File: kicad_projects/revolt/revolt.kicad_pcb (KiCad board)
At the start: 2 copper layers, 144.9 x 111.9 mm, 69 parts, among them J1 IDC-Header_2x07_P2.54mm_Verti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

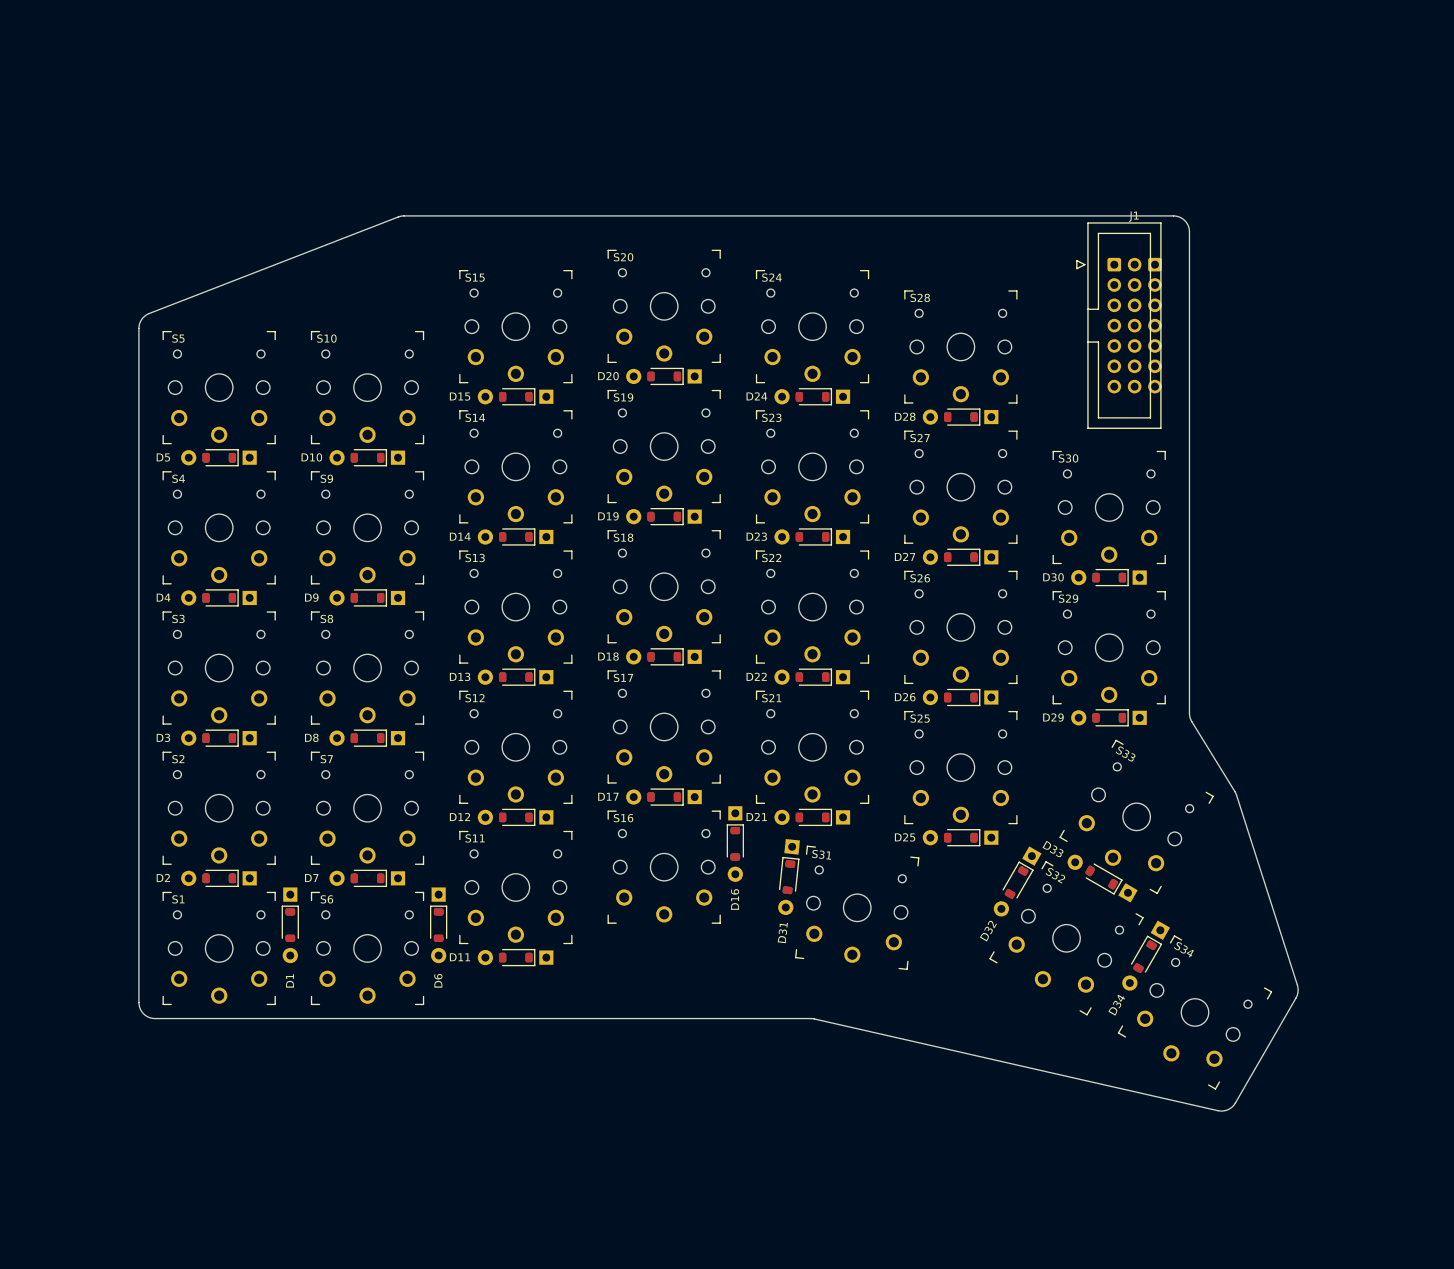
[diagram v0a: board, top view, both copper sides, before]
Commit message: Improved diodes, LED schematic
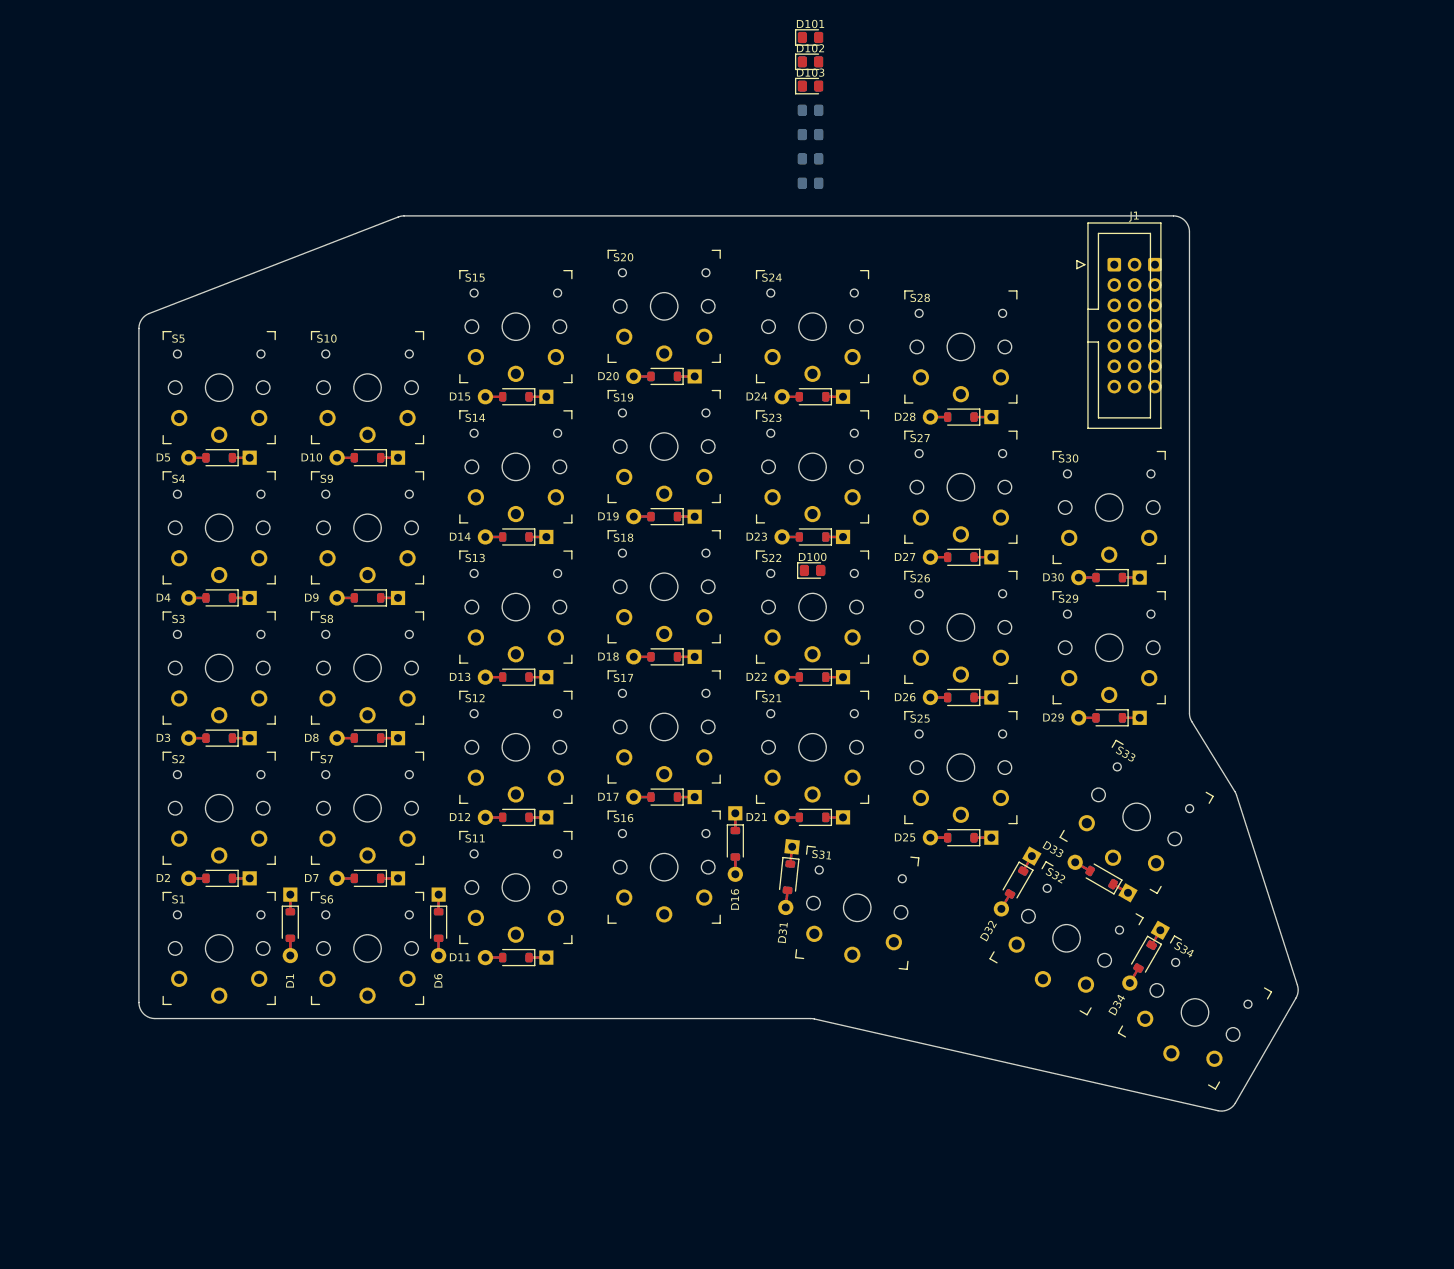
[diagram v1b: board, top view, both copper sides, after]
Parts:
- added D100: LED, LED_SMD:LED_0805_2012Metric_Pad1.15x1.40mm_HandSolder, F.Cu at (175.8, 105.2)
- added D101: LED, LED_SMD:LED_0805_2012Metric_Pad1.15x1.40mm_HandSolder, F.Cu at (175.5, 38.5)
- added D102: LED, LED_SMD:LED_0805_2012Metric_Pad1.15x1.40mm_HandSolder, F.Cu at (175.5, 41.6)
- added D103: LED, LED_SMD:LED_0805_2012Metric_Pad1.15x1.40mm_HandSolder, F.Cu at (175.5, 44.6)
- added D104: LED, LED_SMD:LED_0805_2012Metric_Pad1.15x1.40mm_HandSolder, B.Cu at (175.5, 56.7)
- added D105: LED, LED_SMD:LED_0805_2012Metric_Pad1.15x1.40mm_HandSolder, B.Cu at (175.5, 53.7)
- added D106: LED, LED_SMD:LED_0805_2012Metric_Pad1.15x1.40mm_HandSolder, B.Cu at (175.5, 50.7)
- added D107: LED, LED_SMD:LED_0805_2012Metric_Pad1.15x1.40mm_HandSolder, B.Cu at (175.5, 47.6)

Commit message: Final footprints, schematic fixes, LEDs positioned
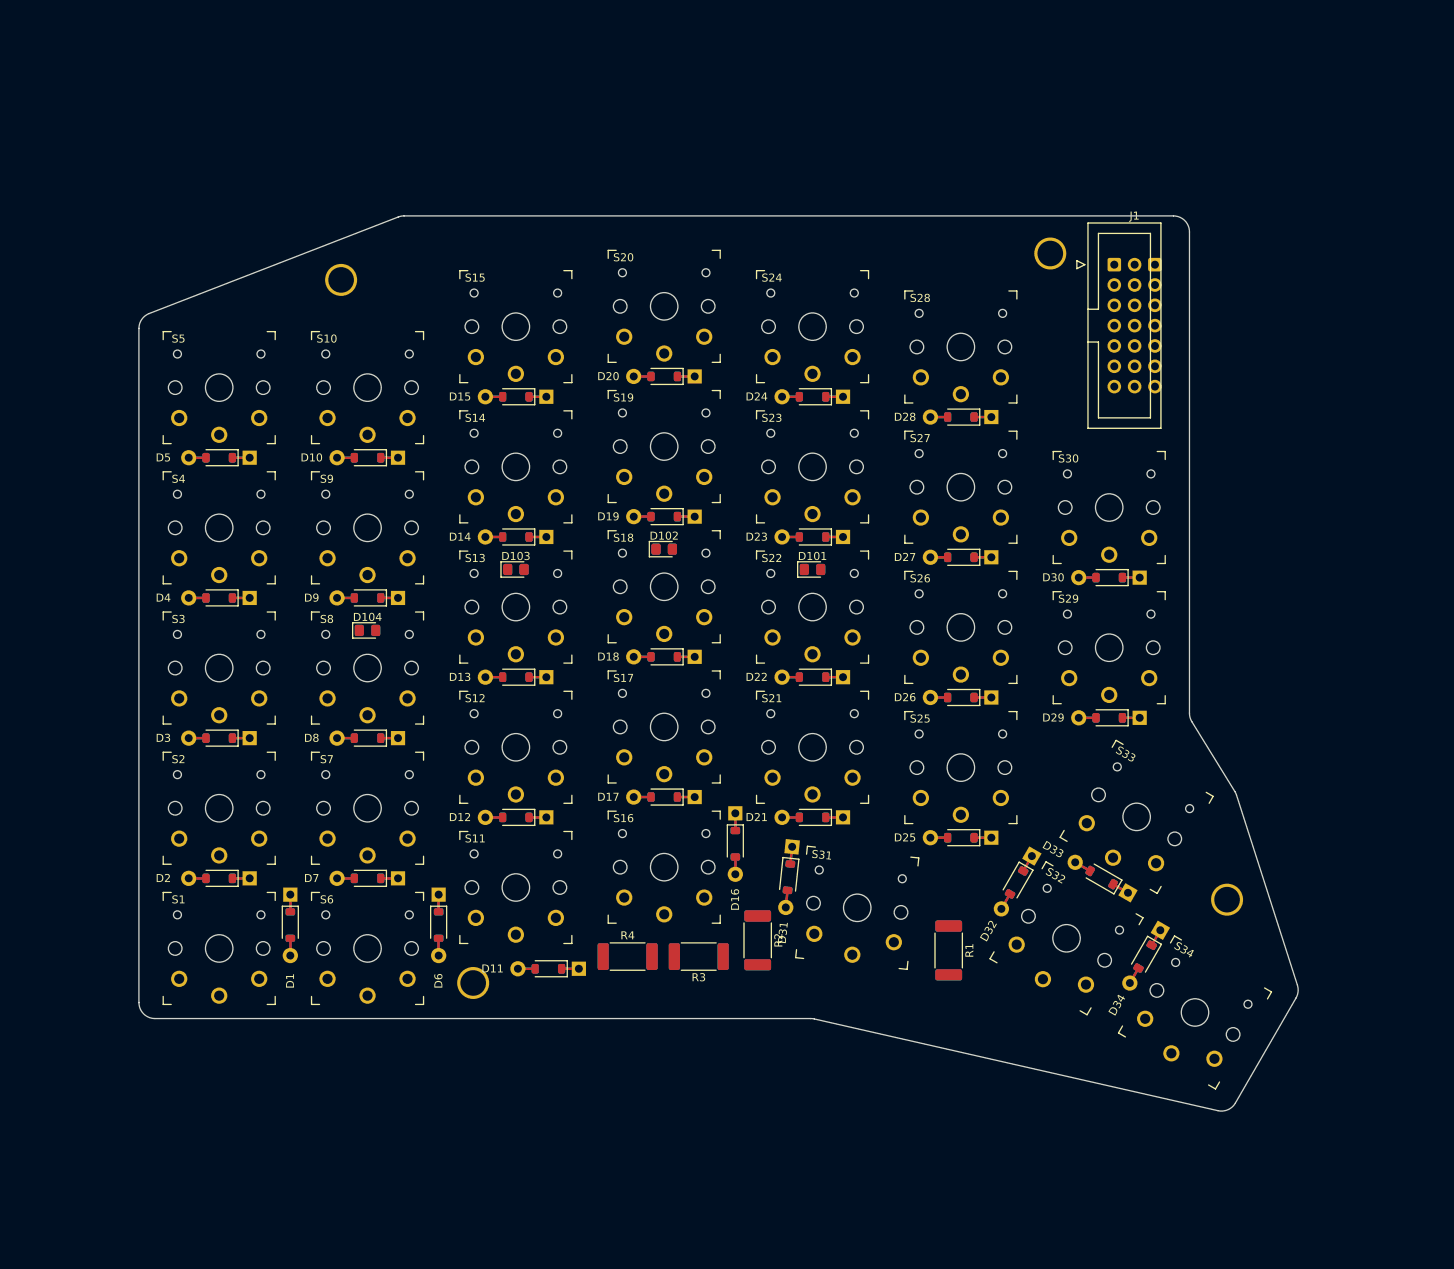
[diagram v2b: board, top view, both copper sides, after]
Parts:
- added H1: MountingHole, revolt_footprints:HOLE_M3, F.Cu at (116.8, 68.8)
- added H2: MountingHole, revolt_footprints:HOLE_M3, F.Cu at (205.5, 65.5)
- added H3: MountingHole, revolt_footprints:HOLE_M3, F.Cu at (227.6, 146.3)
- added H4: MountingHole, revolt_footprints:HOLE_M3, F.Cu at (133.3, 156.7)
- added R1: 150, revolt_footprints:R_2512_6332Metric_Pad1.40x3.35mm_HandSolder_reversible, F.Cu at (192.8, 152.7)
- added R2: 150, revolt_footprints:R_2512_6332Metric_Pad1.40x3.35mm_HandSolder_reversible, F.Cu at (168.9, 151.4)
- added R3: 150, revolt_footprints:R_2512_6332Metric_Pad1.40x3.35mm_HandSolder_reversible, F.Cu at (161.5, 153.4)
- added R4: 150, revolt_footprints:R_2512_6332Metric_Pad1.40x3.35mm_HandSolder_reversible, F.Cu at (152.7, 153.4)
- moved D104 87.7 mm to (120.1, 112.6)
- moved D124 85.4 mm to (120.1, 112.6)
- moved D103 73.4 mm to (138.7, 105.0)
- moved D102 66.5 mm to (157.2, 102.5)
- moved D123 65.7 mm to (138.7, 105.0)
- moved D122 52.1 mm to (157.2, 102.5)
- moved D121 48.3 mm to (175.8, 105.0)
- moved D11 4.30 mm to (142.7, 154.9)
- moved D101 0.13 mm to (175.8, 105.0)
- renumbered D100 to D101, D101 to D102, D102 to D103, D103 to D104, D104 to D121, D105 to D122, D106 to D123, D107 to D124

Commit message: Start routing the board
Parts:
- moved R3 90.1 mm to (128.5, 69.6), turned to 90 degrees
- moved R4 88.7 mm to (123.7, 69.6), turned to 90 degrees
- moved R1 26.9 mm to (165.9, 153.7), turned to 180 degrees
- moved R2 12.2 mm to (157.0, 153.7), turned to 0 degrees
- moved H4 1.02 mm to (134.4, 156.7)
- moved D11 0.92 mm to (143.3, 154.2)
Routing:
- net /COL5: track 0.00 -> 112.2 mm
- net /ROW4: track 0.00 -> 106.2 mm
- net GND: track 0.00 -> 96.8 mm
- net /COL6: track 0.00 -> 92.2 mm, vias 0 -> 1
- net /ROW3: track 0.00 -> 81.7 mm
- net /ROW2: track 0.00 -> 51.7 mm
- net /ROW0: track 0.00 -> 42.1 mm, vias 0 -> 1
- net /ROW1: track 0.00 -> 30.2 mm
- net V5V: track 0.00 -> 20.9 mm
- net Net-(D34-A): track 0.00 -> 16.0 mm
- net Net-(D29-A): track 0.00 -> 14.2 mm
- net Net-(D28-A): track 0.00 -> 14.2 mm
- net Net-(D24-A): track 0.00 -> 14.2 mm
- net Net-(D33-A): track 0.00 -> 14.1 mm
- net /COL0: track 0.00 -> 6.13 mm
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
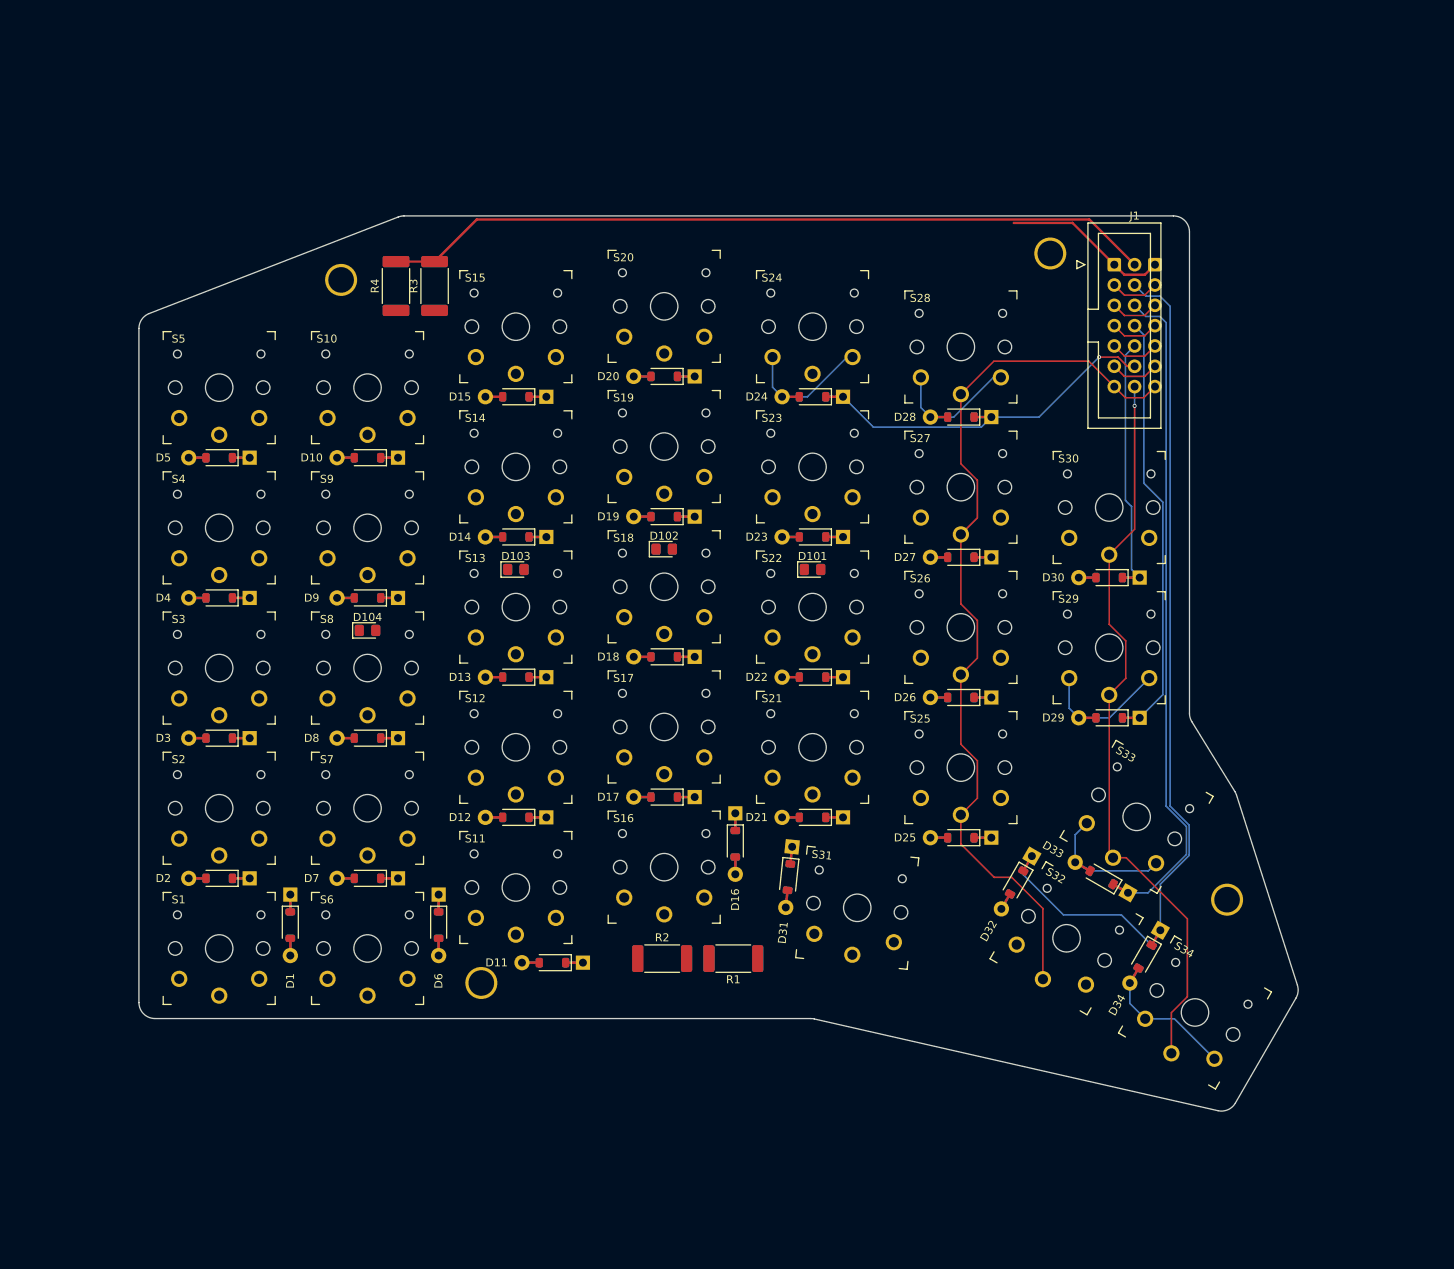
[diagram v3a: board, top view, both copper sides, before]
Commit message: Route everything but the ground plane
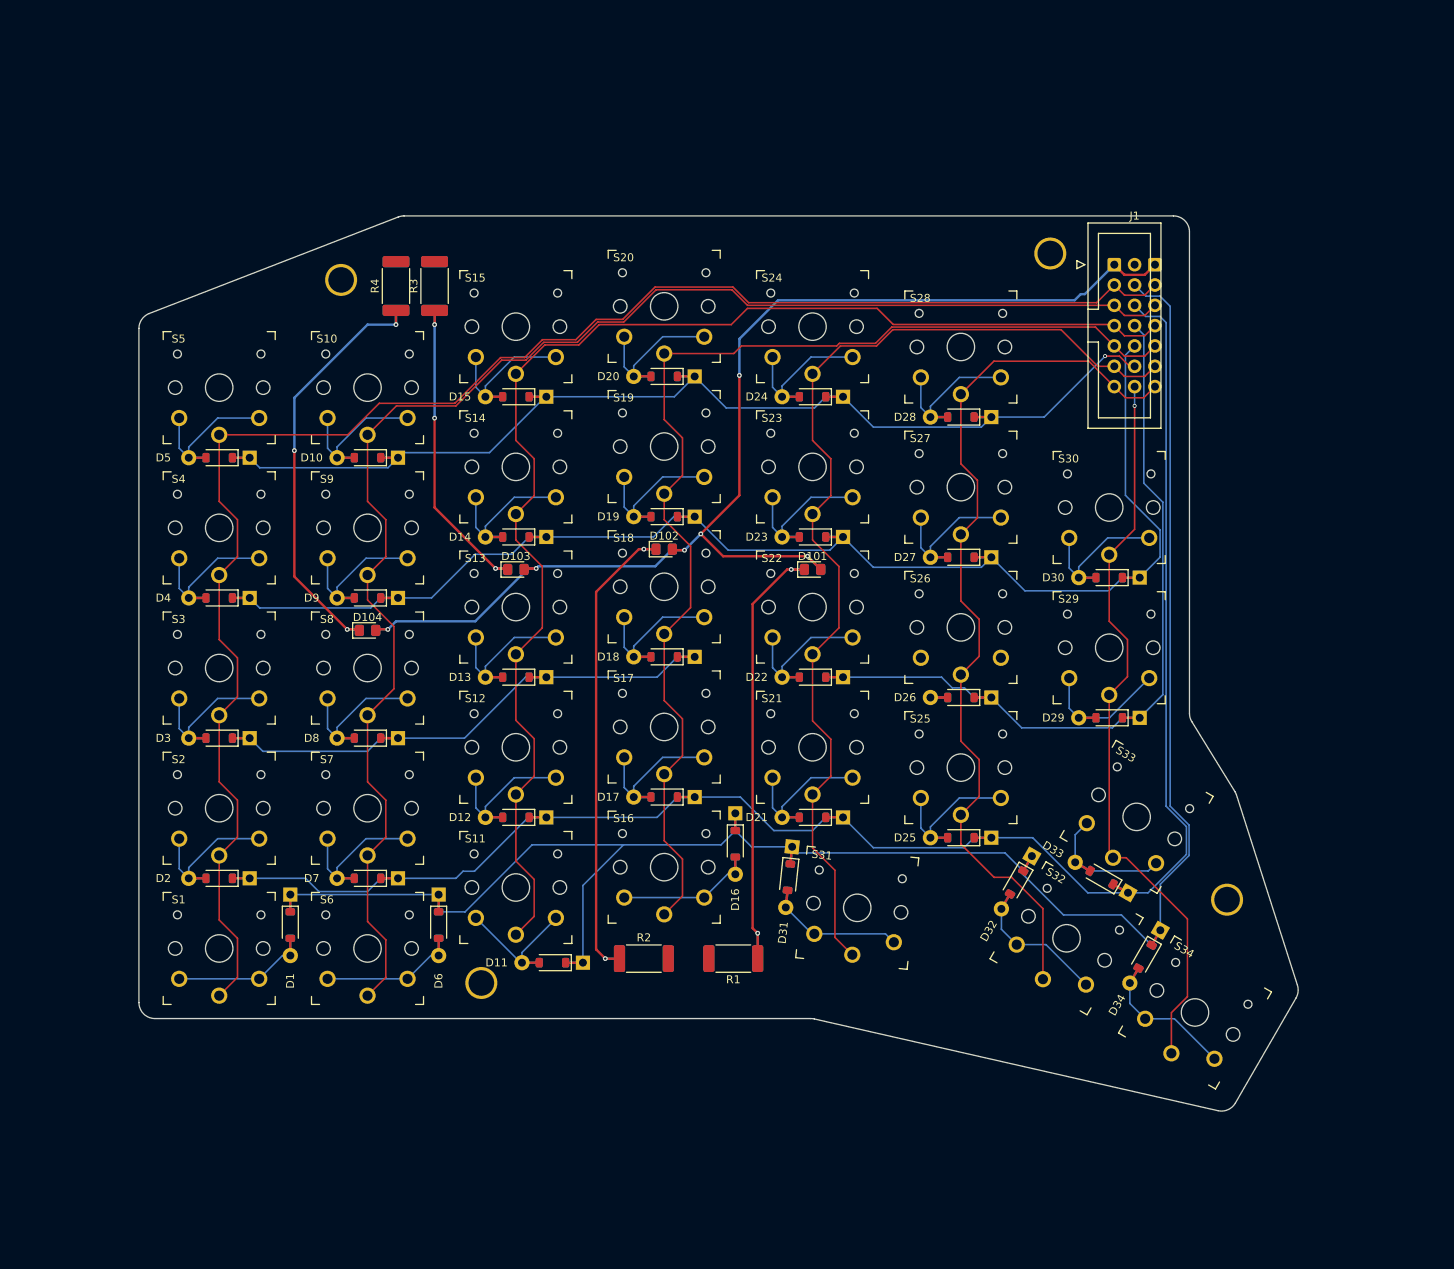
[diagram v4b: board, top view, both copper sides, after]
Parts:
- moved R2 2.29 mm to (154.7, 153.7)
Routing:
- net /COL0: track 6.13 -> 205.1 mm
- net /COL1: track 6.13 -> 186.3 mm
- net /COL2: track 6.13 -> 163.7 mm
- net /COL3: track 6.13 -> 143.3 mm
- net V5V: track 20.9 -> 153.0 mm, vias 0 -> 6
- net /COL4: track 6.13 -> 129.2 mm
- net /ROW1: track 30.2 -> 147.1 mm
- net /ROW4: track 106.2 -> 220.9 mm
- net /ROW3: track 81.7 -> 193.6 mm
- net GND: track 96.8 -> 0.00 mm
- net /ROW2: track 51.7 -> 142.3 mm
- net /ROW0: track 42.1 -> 121.7 mm
- net Net-(D102-K): track 0.00 -> 61.1 mm, vias 0 -> 2
- net Net-(D101-K): track 0.00 -> 57.7 mm, vias 0 -> 2
- net Net-(D104-K): track 0.00 -> 54.9 mm, vias 0 -> 3
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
